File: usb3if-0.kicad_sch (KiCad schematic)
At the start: 16 parts, among them J22 USB3_A, U33 AP22652W6-7, U34 RCLAMP0524P, U35 RCLAMP0524P

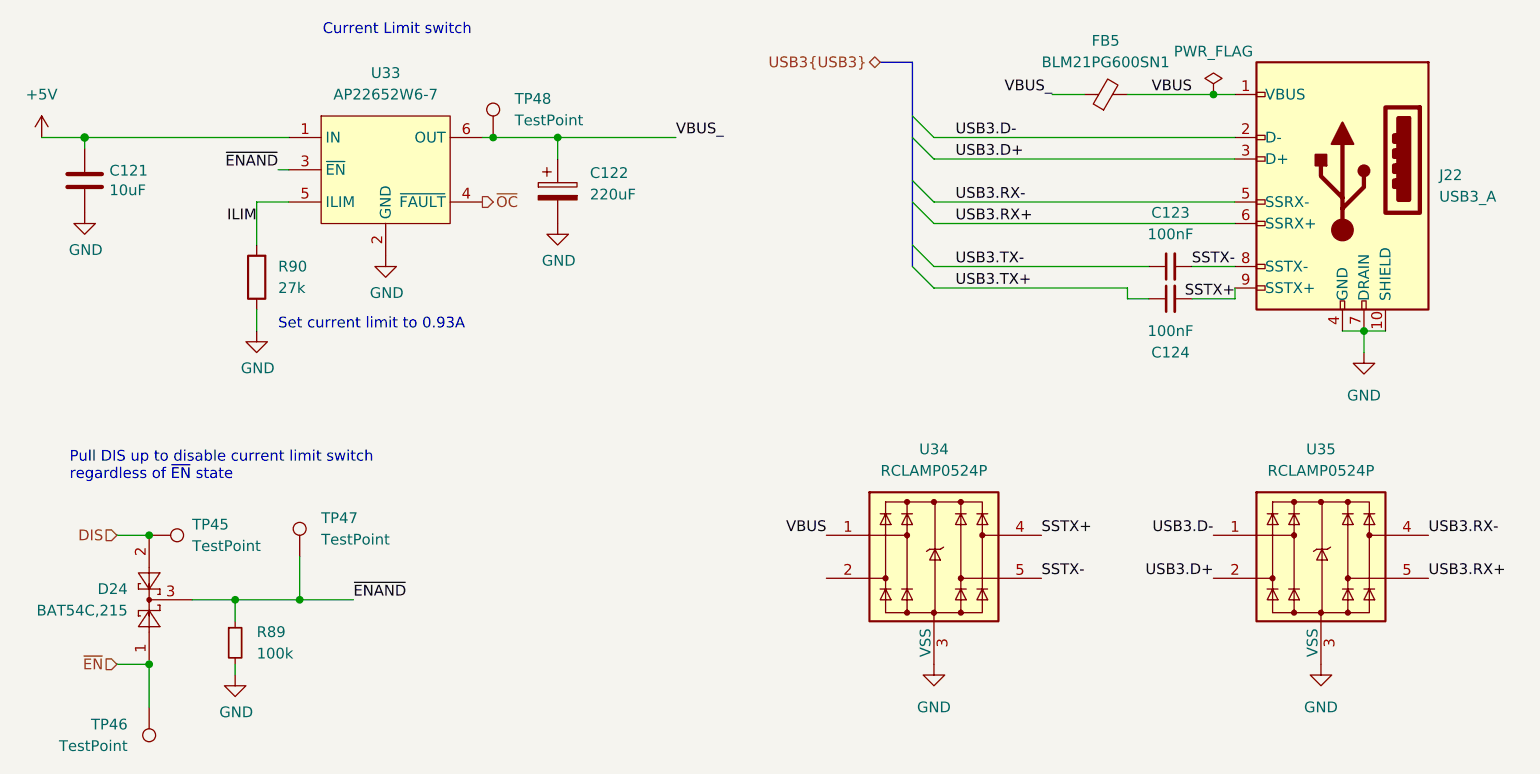
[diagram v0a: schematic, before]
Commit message: Add the missing capacitors to the USB3 hub RX diff pairs
Also adjust RS485 auto-enable resistor sizes and remove the
extra USB3-0 diff pair caps
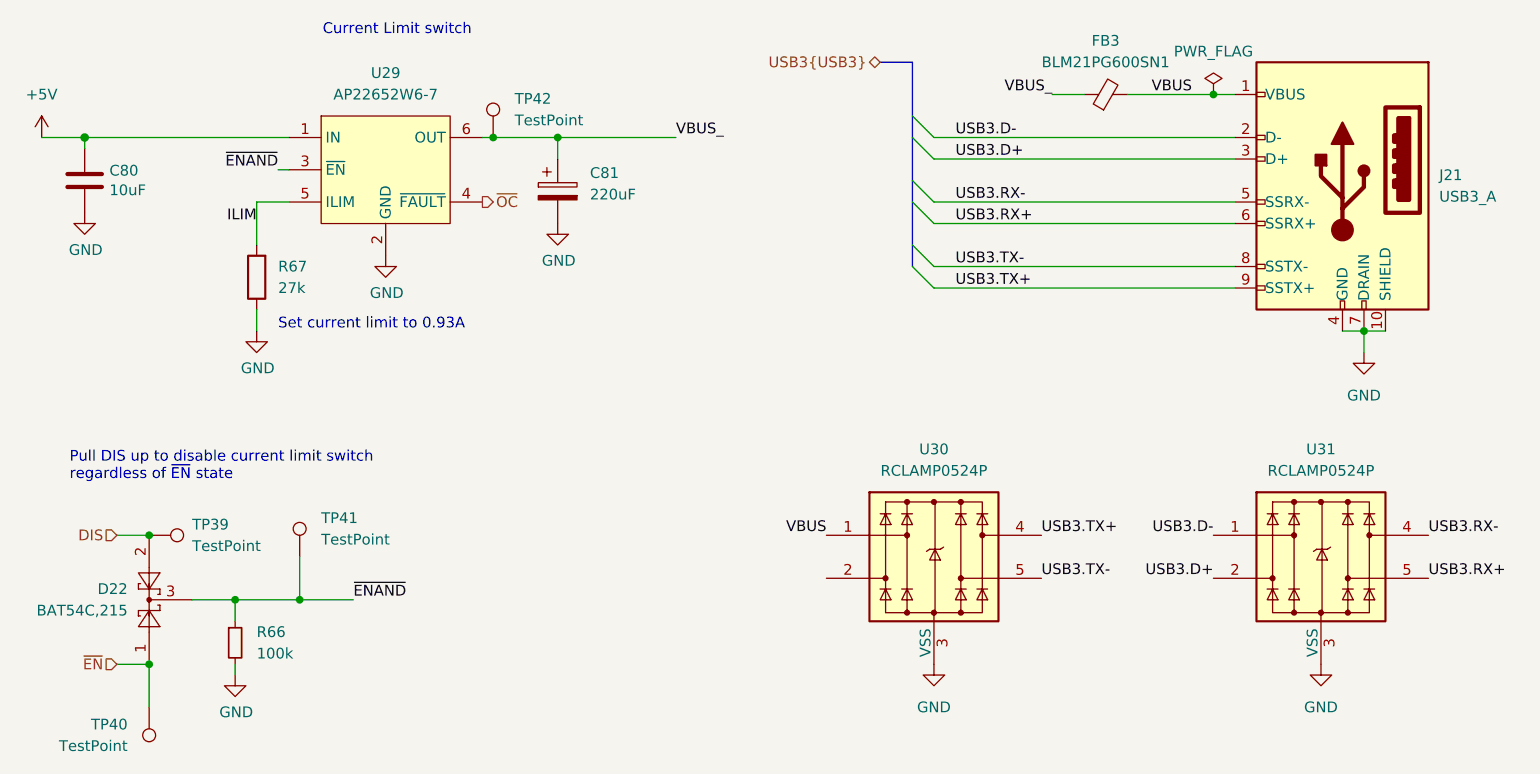
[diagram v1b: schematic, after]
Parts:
- removed C123, C124: 100nF, Capacitor_SMD:C_0201_0603Metric, symbol Device:C_Small
- renumbered C121 to C80, C122 to C81, D24 to D22, FB5 to FB3, J22 to J21, R89 to R66, R90 to R67, TP45 to TP39, TP46 to TP40, TP47 to TP41, TP48 to TP42, U33 to U29, U34 to U30, U35 to U31
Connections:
- net SSTX+ is gone; now on net USB3.TX+: J21.9 (SSTX+), U30.4, U30.7
- net SSTX- is gone; now on net USB3.TX-: J21.8 (SSTX-), U30.5, U30.6
